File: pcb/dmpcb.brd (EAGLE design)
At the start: 100 x 100 mm, 63 parts, among them IC1 7805DT, IC2 L293D, IC3 MAX7219CNG, IC4 LM358D, IC5 LM358D, J7 SJ-3523-SMT-TR, Q1 IRF530, Q2 IRF530

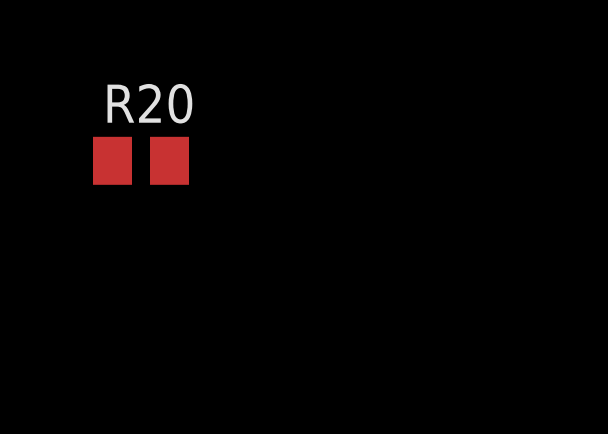
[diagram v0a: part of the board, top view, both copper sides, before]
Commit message: added missing decoupling cap
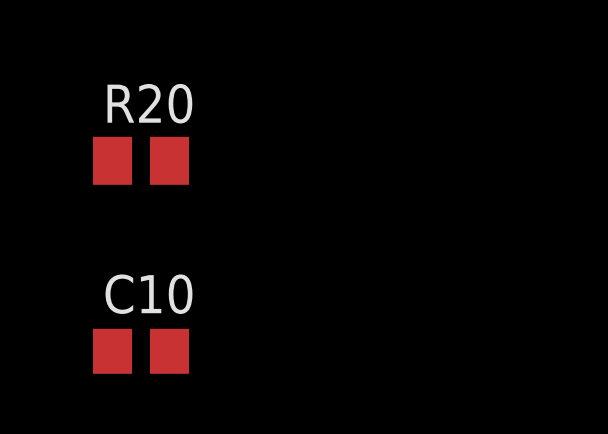
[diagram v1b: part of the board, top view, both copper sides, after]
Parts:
- added C10: 100nf, rcl:C0805
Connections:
- net +5V: now also C10.2
- net GND: now also C10.1
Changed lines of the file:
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@@
 <attribute name="VALUE" x="-109.982" y="-76.454" size="1.27" layer="27" ratio="10"/>
+</element>
+<element name="C10" library="rcl" library_urn="urn:adsk.eagle:library:334" package="C0805" package3d_urn="urn:adsk.eagle:package:23617/2" value="100nf" x="-107.95" y="-87.63" smashed="yes">
+<attribute name="NAME" x="-109.22" y="-86.36" size="1.27" layer="25"/>
+<attribute name="SPICEPREFIX" value="C" x="-107.95" y="-87.63" size="1.778" layer="27" display="off"/>
+<attribute name="VALUE" x="-109.22" y="-90.17" size="1.27" layer="27"/>
 </element>
 </elements>
@@
 <contactref element="R19" pad="A"/>
 <contactref element="J7" pad="1"/>
+<contactref element="C10" pad="1"/>
+<wire x1="-107" y1="-81.28" x2="-108.9" y2="-87.63" width="0" layer="19" extent="1-1"/>
 <wire x1="-105.24" y1="-54.5" x2="-107" y2="-81.28" width="0" layer="19" extent="1-1"/>
 <wire x1="-87.63" y1="-37.465" x2="-105.24" y2="-54.5" width="0" layer="19" extent="1-1"/>
@@
 <contactref element="J5" pad="5"/>
 <contactref element="IC5" pad="8"/>
-<wire x1="77.47" y1="15.24" x2="54.61" y2="72.39" width="0" layer="19" extent="1-1"/>
-<wire x1="42.18" y1="2.54" x2="77.47" y2="15.24" width="0" layer="19" extent="1-1"/>
-<wire x1="25.14" y1="5.36" x2="42.18" y2="2.54" width="0" layer="19" extent="1-1"/>
-<wire x1="11.43" y1="7.62" x2="25.14" y2="5.36" width="0" layer="19" extent="1-1"/>
-<wire x1="-39.37" y1="44.45" x2="11.43" y2="7.62" width="0" layer="19" extent="1-1"/>
-<wire x1="-40.31" y1="66.04" x2="-39.37" y2="44.45" width="0" layer="19" extent="1-1"/>
-<wire x1="-44.13" y1="73.66" x2="-40.31" y2="66.04" width="0" layer="19" extent="1-1"/>
-<wire x1="-48.78" y1="73.66" x2="-44.13" y2="73.66" width="0" layer="19" extent="1-1"/>
-<wire x1="-62.45" y1="78.74" x2="-48.78" y2="73.66" width="0" layer="19" extent="1-1"/>
+<contactref element="C10" pad="2"/>
+<wire x1="-93.345" y1="-26.61" x2="-107" y2="-87.63" width="0" layer="19" extent="1-1"/>
+<wire x1="-76.2" y1="40.64" x2="-93.345" y2="-26.61" width="0" layer="19" extent="1-1"/>
+<wire x1="-80.01" y1="52.07" x2="-76.2" y2="40.64" width="0" layer="19" extent="1-1"/>
+<wire x1="-62.45" y1="78.74" x2="-80.01" y2="52.07" width="0" layer="19" extent="1-1"/>
+<wire x1="-48.78" y1="73.66" x2="-62.45" y2="78.74" width="0" layer="19" extent="1-1"/>
+<wire x1="-44.13" y1="73.66" x2="-48.78" y2="73.66" width="0" layer="19" extent="1-1"/>
+<wire x1="-40.31" y1="66.04" x2="-44.13" y2="73.66" width="0" layer="19" extent="1-1"/>
+<wire x1="-39.37" y1="44.45" x2="-40.31" y2="66.04" width="0" layer="19" extent="1-1"/>
 <wire x1="-14.29" y1="80.01" x2="-40.31" y2="66.04" width="0" layer="19" extent="1-1"/>
-<wire x1="-80.01" y1="52.07" x2="-62.45" y2="78.74" width="0" layer="19" extent="1-1"/>
-<wire x1="-76.2" y1="40.64" x2="-80.01" y2="52.07" width="0" layer="19" extent="1-1"/>
 <wire x1="4.445" y1="110.55" x2="-14.29" y2="80.01" width="0" layer="19" extent="1-1"/>
 <wire x1="-52.07" y1="121.92" x2="-62.45" y2="78.74" width="0" layer="19" extent="1-1"/>
-<wire x1="-93.345" y1="-26.61" x2="-76.2" y2="40.64" width="0" layer="19" extent="1-1"/>
+<wire x1="11.43" y1="7.62" x2="-39.37" y2="44.45" width="0" layer="19" extent="1-1"/>
+<wire x1="25.14" y1="5.36" x2="11.43" y2="7.62" width="0" layer="19" extent="1-1"/>
+<wire x1="42.18" y1="2.54" x2="25.14" y2="5.36" width="0" layer="19" extent="1-1"/>
+<wire x1="77.47" y1="15.24" x2="42.18" y2="2.54" width="0" layer="19" extent="1-1"/>
+<wire x1="54.61" y1="72.39" x2="77.47" y2="15.24" width="0" layer="19" extent="1-1"/>
 </signal>
 <signal name="G">

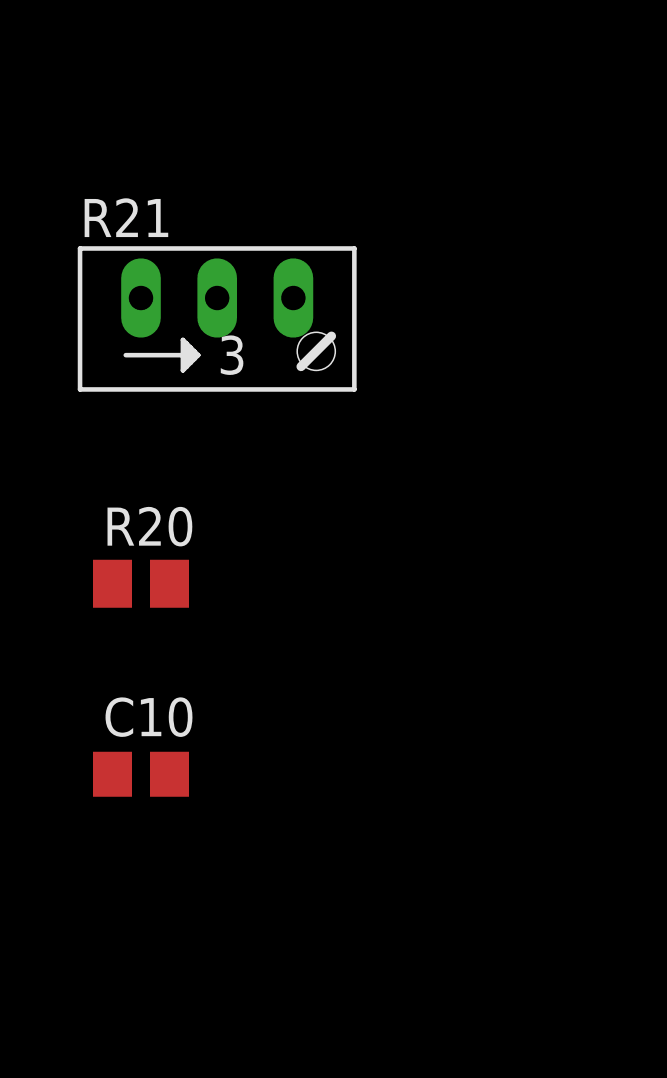
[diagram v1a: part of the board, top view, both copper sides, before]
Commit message: corrected sensorport and changed the second half of the lm358 to a freely user-configurable setup
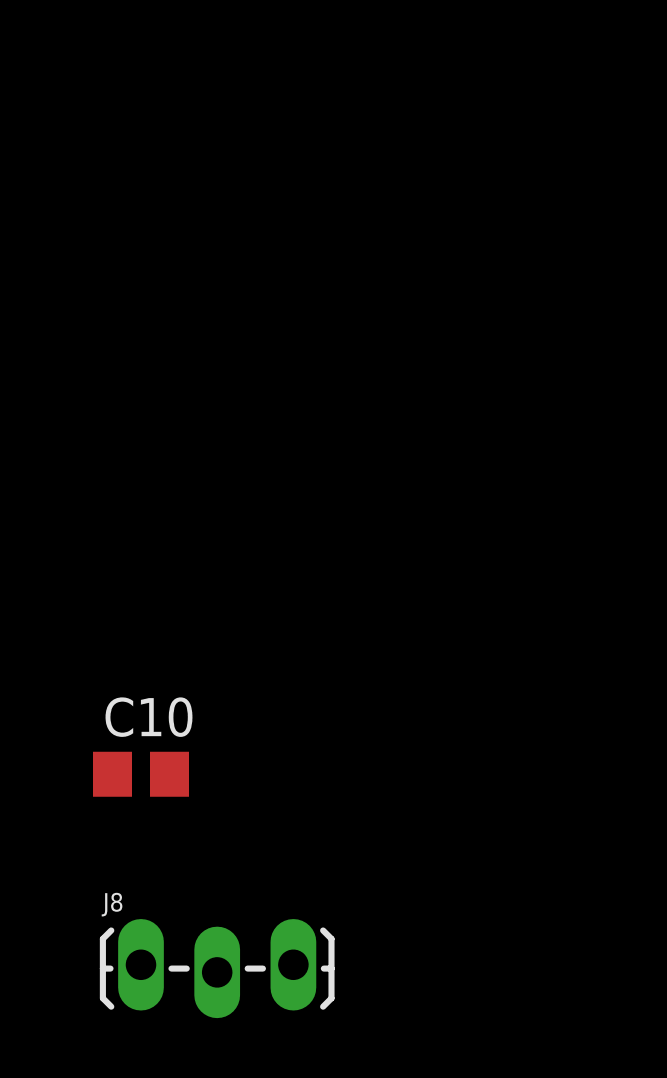
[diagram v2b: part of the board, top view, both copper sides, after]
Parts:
- removed R20: 10K, rcl:M0805
- removed R21: b100k, pot:RJ9W
- added J8: (no value), SparkFun-Connectors:1X03_LOCK_LONGPADS
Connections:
- new net N$70: IC4.6, J8.2
- net +5V: now also SENSOR.P2
- net GND: now also JP3.2, JP3.4, JP3.6; no longer R20.2, SENSOR.P2
- net N$20: now also IC4.5, J8.3; no longer R10.2, R11.2, R9.2, SENSOR.P1
- net N$75: now also IC4.7, J8.1; no longer IC4.6, R20.1, R21.A
- net OPAMPIN: no longer IC4.5
- net OPAMPOUT: no longer IC4.7, R21.E, R21.S
- net SENSORPORT: now also R10.2, R11.2, R9.2, SENSOR.P1; no longer JP3.2, JP3.4, JP3.6
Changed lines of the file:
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@@
 <attribute name="VALUE" x="-107.34573125" y="-57.41181875" size="1.27228125" layer="27"/>
-</element>
-<element name="R20" library="rcl" library_urn="urn:adsk.eagle:library:334" package="M0805" package3d_urn="urn:adsk.eagle:package:23556/1" value="10K" x="-107.95" y="-81.28" smashed="yes">
-<attribute name="NAME" x="-109.22" y="-80.01" size="1.27" layer="25"/>
-<attribute name="SPICEPREFIX" value="R" x="-116.84" y="-62.23" size="1.778" layer="27" display="off"/>
-<attribute name="VALUE" x="-109.22" y="-83.82" size="1.27" layer="27"/>
-</element>
-<element name="R21" library="pot" library_urn="urn:adsk.eagle:library:331" package="RJ9W" package3d_urn="urn:adsk.eagle:package:22702/1" value="b100k" x="-105.41" y="-72.39" smashed="yes">
-<attribute name="NAME" x="-109.982" y="-69.723" size="1.27" layer="25" ratio="10"/>
-<attribute name="VALUE" x="-109.982" y="-76.454" size="1.27" layer="27" ratio="10"/>
 </element>
 <element name="C10" library="rcl" library_urn="urn:adsk.eagle:library:334" package="C0805" package3d_urn="urn:adsk.eagle:package:23617/2" value="100nf" x="-107.95" y="-87.63" smashed="yes">
@@
 <attribute name="SPICEPREFIX" value="C" x="-107.95" y="-87.63" size="1.778" layer="27" display="off"/>
 <attribute name="VALUE" x="-109.22" y="-90.17" size="1.27" layer="27"/>
+</element>
+<element name="J8" library="SparkFun-Connectors" library_urn="urn:adsk.eagle:library:513" package="1X03_LOCK_LONGPADS" package3d_urn="urn:adsk.eagle:package:38065/1" value="" x="-107.95" y="-93.98" smashed="yes">
+<attribute name="NAME" x="-109.22" y="-92.202" size="0.6096" layer="25" font="vector" ratio="20"/>
+<attribute name="VALUE" x="-109.22" y="-96.393" size="0.6096" layer="27" font="vector" ratio="20"/>
 </element>
 </elements>
@@
 <contactref element="R7" pad="2"/>
 <contactref element="R8" pad="2"/>
-<contactref element="SENSOR" pad="P2"/>
 <contactref element="R12" pad="1"/>
 <contactref element="R13" pad="1"/>
@@
 <contactref element="J6" pad="4"/>
 <contactref element="J6" pad="5"/>
-<contactref element="R20" pad="2"/>
 <contactref element="IC5" pad="4"/>
 <contactref element="C4" pad="2"/>
@@
 <contactref element="J7" pad="1"/>
 <contactref element="C10" pad="1"/>
-<wire x1="-107" y1="-81.28" x2="-108.9" y2="-87.63" width="0" layer="19" extent="1-1"/>
-<wire x1="-105.24" y1="-54.5" x2="-107" y2="-81.28" width="0" layer="19" extent="1-1"/>
+<contactref element="JP3" pad="2"/>
+<contactref element="JP3" pad="4"/>
+<contactref element="JP3" pad="6"/>
+<wire x1="-105.24" y1="-54.5" x2="-108.9" y2="-87.63" width="0" layer="19" extent="1-1"/>
 <wire x1="-87.63" y1="-37.465" x2="-105.24" y2="-54.5" width="0" layer="19" extent="1-1"/>
 <wire x1="-89.535" y1="-31.81" x2="-87.63" y2="-37.465" width="0" layer="19" extent="1-1"/>
@@
 <wire x1="-81.28" y1="40.64" x2="-58.74" y2="35.56" width="0" layer="19" extent="1-1"/>
 <wire x1="-85.09" y1="52.07" x2="-81.28" y2="40.64" width="0" layer="19" extent="1-1"/>
-<wire x1="-72.07" y1="73.66" x2="-85.09" y2="52.07" width="0" layer="19" extent="1-1"/>
-<wire x1="-66.99" y1="73.66" x2="-72.07" y2="73.66" width="0" layer="19" extent="1-1"/>
-<wire x1="-56.83" y1="73.66" x2="-66.99" y2="73.66" width="0" layer="19" extent="1-1"/>
-<wire x1="-50.28" y1="73.66" x2="-56.83" y2="73.66" width="0" layer="19" extent="1-1"/>
-<wire x1="-42.23" y1="73.66" x2="-50.28" y2="73.66" width="0" layer="19" extent="1-1"/>
+<wire x1="-20.32" y1="58.42" x2="-31.75" y2="36.83" width="0" layer="19" extent="1-1"/>
+<wire x1="-17.78" y1="58.42" x2="-20.32" y2="58.42" width="0" layer="19" extent="1-1"/>
+<wire x1="-15.24" y1="58.42" x2="-17.78" y2="58.42" width="0" layer="19" extent="1-1"/>
+<wire x1="-18.53" y1="73.66" x2="-17.78" y2="58.42" width="0" layer="19" extent="1-1"/>
+<wire x1="-29.53" y1="73.66" x2="-18.53" y2="73.66" width="0" layer="19" extent="1-1"/>
+<wire x1="-42.23" y1="73.66" x2="-29.53" y2="73.66" width="0" layer="19" extent="1-1"/>
 <wire x1="-43.18" y1="80.01" x2="-42.23" y2="73.66" width="0" layer="19" extent="1-1"/>
 <wire x1="-43.51" y1="66.04" x2="-42.23" y2="73.66" width="0" layer="19" extent="1-1"/>
-<wire x1="-29.53" y1="73.66" x2="-42.23" y2="73.66" width="0" layer="19" extent="1-1"/>
-<wire x1="-18.53" y1="73.66" x2="-29.53" y2="73.66" width="0" layer="19" extent="1-1"/>
+<wire x1="-50.28" y1="73.66" x2="-42.23" y2="73.66" width="0" layer="19" extent="1-1"/>
+<wire x1="-56.83" y1="73.66" x2="-50.28" y2="73.66" width="0" layer="19" extent="1-1"/>
+<wire x1="-66.99" y1="73.66" x2="-56.83" y2="73.66" width="0" layer="19" extent="1-1"/>
+<wire x1="-72.07" y1="73.66" x2="-66.99" y2="73.66" width="0" layer="19" extent="1-1"/>
 <wire x1="15.24" y1="82.55" x2="-18.53" y2="73.66" width="0" layer="19" extent="1-1"/>
 <wire x1="8.255" y1="105.35" x2="15.24" y2="82.55" width="0" layer="19" extent="1-1"/>
@@
 <wire x1="49.8" y1="20.32" x2="49.8" y2="35.56" width="0" layer="19" extent="1-1"/>
 <wire x1="57.42" y1="2.54" x2="49.8" y2="20.32" width="0" layer="19" extent="1-1"/>
-<wire x1="96.52" y1="53.34" x2="73.66" y2="55.88" width="0" layer="19" extent="1-1"/>
 <wire x1="77.47" y1="22.86" x2="49.8" y2="20.32" width="0" layer="19" extent="1-1"/>
 <wire x1="77.47" y1="25.4" x2="77.47" y2="22.86" width="0" layer="19" extent="1-1"/>
@@
 <contactref element="IC5" pad="8"/>
 <contactref element="C10" pad="2"/>
+<contactref element="SENSOR" pad="P2"/>
 <wire x1="-93.345" y1="-26.61" x2="-107" y2="-87.63" width="0" layer="19" extent="1-1"/>
 <wire x1="-76.2" y1="40.64" x2="-93.345" y2="-26.61" width="0" layer="19" extent="1-1"/>
@@
 <wire x1="42.18" y1="2.54" x2="25.14" y2="5.36" width="0" layer="19" extent="1-1"/>
 <wire x1="77.47" y1="15.24" x2="42.18" y2="2.54" width="0" layer="19" extent="1-1"/>
-<wire x1="54.61" y1="72.39" x2="77.47" y2="15.24" width="0" layer="19" extent="1-1"/>
+<wire x1="96.52" y1="53.34" x2="77.47" y2="15.24" width="0" layer="19" extent="1-1"/>
+<wire x1="54.61" y1="72.39" x2="96.52" y2="53.34" width="0" layer="19" extent="1-1"/>
 </signal>
 <signal name="G">
@@
 <wire x1="-20.32" y1="55.88" x2="-21.27" y2="80.01" width="0" layer="19" extent="1-1"/>
 </signal>
-<signal name="N$20">
+<signal name="SENSORPORT">
+<contactref element="J4" pad="18"/>
+<contactref element="J4" pad="11"/>
 <contactref element="R10" pad="2"/>
 <contactref element="SENSOR" pad="P1"/>
 <contactref element="R9" pad="2"/>
 <contactref element="R11" pad="2"/>
+<wire x1="64.77" y1="45.72" x2="96.52" y2="50.8" width="0" layer="19" extent="1-1"/>
+<wire x1="64.77" y1="27.94" x2="64.77" y2="45.72" width="0" layer="19" extent="1-1"/>
+<wire x1="-19.37" y1="80.01" x2="64.77" y2="45.72" width="0" layer="19" extent="1-1"/>
 <wire x1="-34.61" y1="80.01" x2="-19.37" y2="80.01" width="0" layer="19" extent="1-1"/>
-<wire x1="96.52" y1="50.8" x2="-34.61" y2="80.01" width="0" layer="19" extent="1-1"/>
 <wire x1="-60.01" y1="73.66" x2="-34.61" y2="80.01" width="0" layer="19" extent="1-1"/>
-</signal>
-<signal name="SENSORPORT">
-<contactref element="JP3" pad="2"/>
-<contactref element="JP3" pad="4"/>
-<contactref element="JP3" pad="6"/>
-<contactref element="J4" pad="18"/>
-<contactref element="J4" pad="11"/>
-<wire x1="64.77" y1="27.94" x2="64.77" y2="45.72" width="0" layer="19" extent="1-1"/>
-<wire x1="-15.24" y1="58.42" x2="64.77" y2="45.72" width="0" layer="19" extent="1-1"/>
-<wire x1="-17.78" y1="58.42" x2="-15.24" y2="58.42" width="0" layer="19" extent="1-1"/>
-<wire x1="-20.32" y1="58.42" x2="-17.78" y2="58.42" width="0" layer="19" extent="1-1"/>
 </signal>
 <signal name="BUTTON01">
@@
 <signal name="OPAMPIN">
 <contactref element="IC4" pad="3"/>
-<contactref element="IC4" pad="5"/>
-<wire x1="6.985" y1="105.35" x2="8.255" y2="110.55" width="0" layer="19" extent="1-1"/>
 </signal>
 <signal name="OPAMPOUT">
@@
 <contactref element="R15" pad="E"/>
 <contactref element="R15" pad="S"/>
-<contactref element="R21" pad="S"/>
-<contactref element="R21" pad="E"/>
-<contactref element="IC4" pad="7"/>
-<wire x1="-105.41" y1="-71.755" x2="-107.95" y2="-71.755" width="0" layer="19" extent="1-1"/>
-<wire x1="-83.82" y1="-4.445" x2="-105.41" y2="-71.755" width="0" layer="19" extent="1-1"/>
-<wire x1="-81.28" y1="-4.445" x2="-83.82" y2="-4.445" width="0" layer="19" extent="1-1"/>
-<wire x1="4.445" y1="105.35" x2="-81.28" y2="-4.445" width="0" layer="19" extent="1-1"/>
-<wire x1="5.715" y1="110.55" x2="4.445" y2="105.35" width="0" layer="19" extent="1-1"/>
 <wire x1="64.77" y1="25.4" x2="4.445" y2="105.35" width="0" layer="19" extent="1-1"/>
+<wire x1="-81.28" y1="-4.445" x2="4.445" y2="105.35" width="0" layer="19" extent="1-1"/>
+<wire x1="-83.82" y1="-4.445" x2="-81.28" y2="-4.445" width="0" layer="19" extent="1-1"/>
 </signal>
 <signal name="N$63">
@@
 <wire x1="-106.35" y1="-38.1" x2="-103.24" y2="-47.1" width="0" layer="19" extent="1-1"/>
 </signal>
+<signal name="N$20">
+<contactref element="IC4" pad="5"/>
+<contactref element="J8" pad="3"/>
+<wire x1="8.255" y1="110.55" x2="-102.87" y2="-93.98" width="0" layer="19" extent="1-1"/>
+</signal>
+<signal name="N$70">
+<contactref element="IC4" pad="6"/>
+<contactref element="J8" pad="2"/>
+<wire x1="6.985" y1="110.55" x2="-105.41" y2="-94.234" width="0" layer="19" extent="1-1"/>
+</signal>
 <signal name="N$75">
-<contactref element="R20" pad="1"/>
-<contactref element="R21" pad="A"/>
-<contactref element="IC4" pad="6"/>
-<wire x1="-102.87" y1="-71.755" x2="-108.9" y2="-81.28" width="0" layer="19" extent="1-1"/>
-<wire x1="6.985" y1="110.55" x2="-102.87" y2="-71.755" width="0" layer="19" extent="1-1"/>
+<contactref element="J8" pad="1"/>
+<contactref element="IC4" pad="7"/>
+<wire x1="5.715" y1="110.55" x2="-107.95" y2="-93.98" width="0" layer="19" extent="1-1"/>
 </signal>
 </signals>
